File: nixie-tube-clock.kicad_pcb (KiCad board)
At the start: 2 copper layers, 157.5 x 72 mm, 137 parts, among them IC1 TPS61041DBVR, IC2 UCC3803DTR, J5 USB4105-GF-A, J7 DEBUG, Q1 MMBT42, Q2 FDS2672CT, SW1 SW_SPST, U1 CD40109BPW, U2 W25Q32JV, U3 RP2350A, U4 MCP1702T-3302E_CB, U5 CD40109BPW, U6 HV5122PG-G, U7 HV5122PG-G, U8 DS3231M, X1 IQXO-791

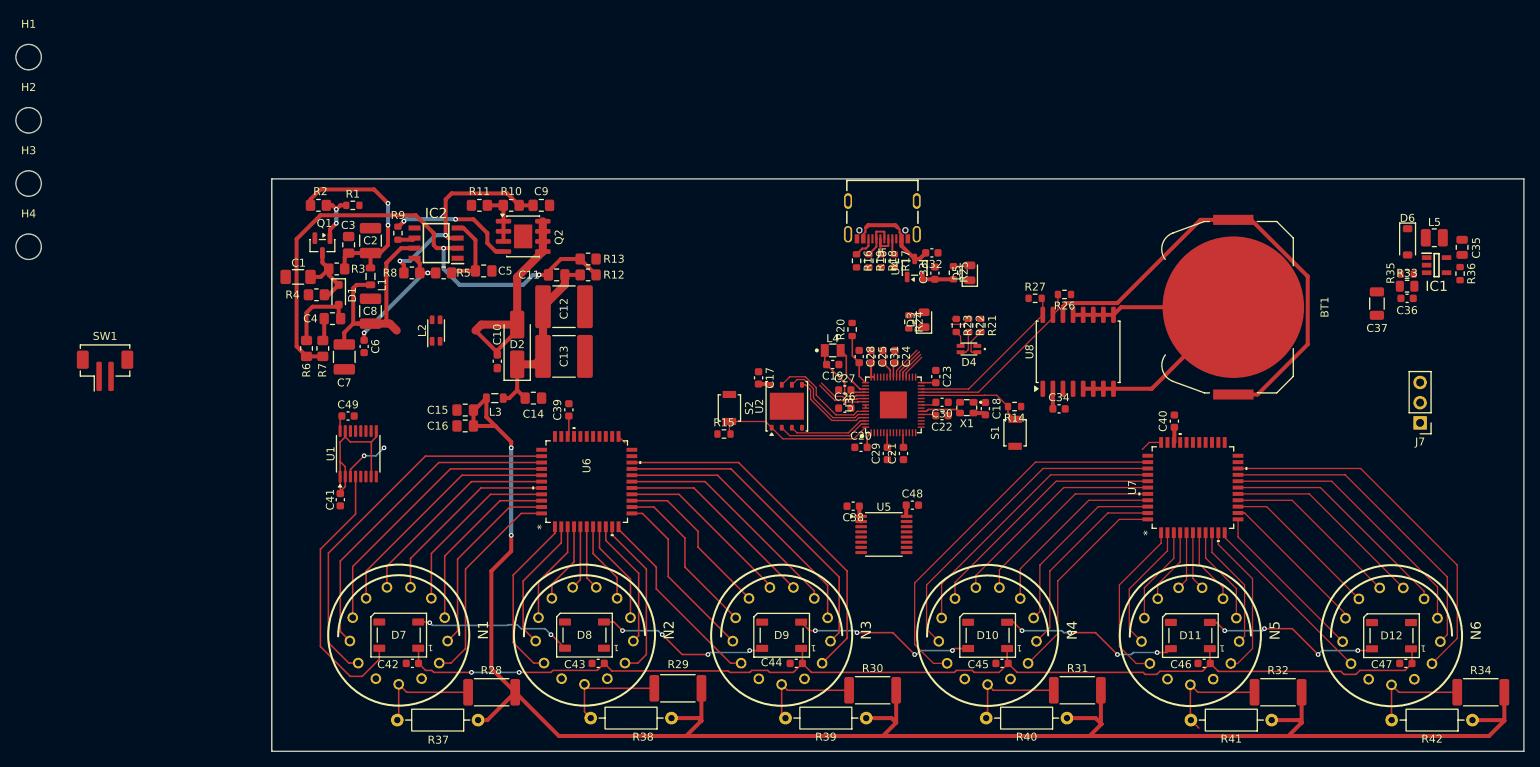
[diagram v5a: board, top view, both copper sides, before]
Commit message: Complete layout first pass
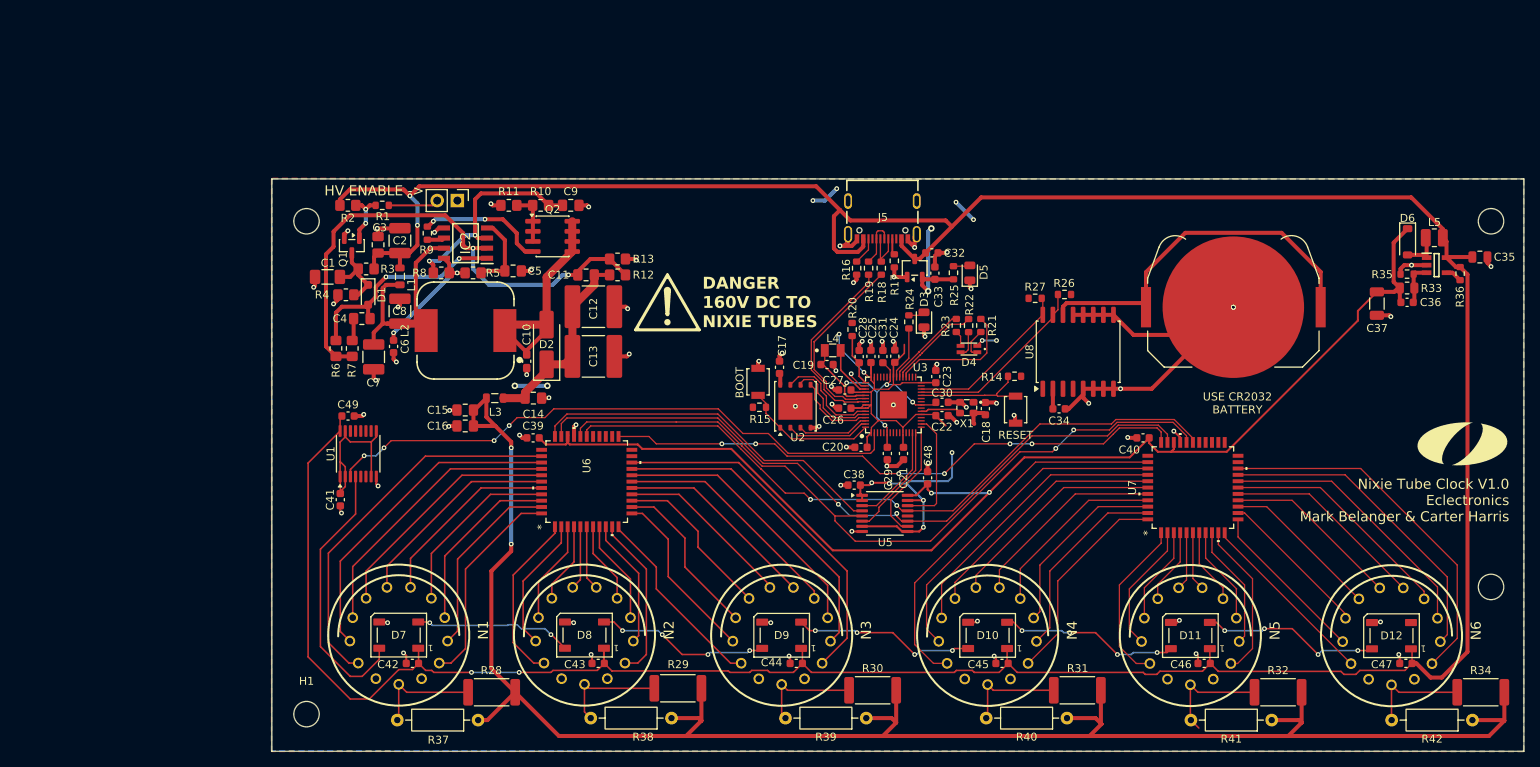
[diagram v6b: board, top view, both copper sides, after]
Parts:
- removed J7: DEBUG, Connector_PinHeader_2.54mm:PinHeader_1x03_P2.54mm_Vertical
- removed S1: RST, Button_Switch_SMD:SW_SPST_B3U-1000P
- removed S2: BOOT, Button_Switch_SMD:SW_SPST_B3U-1000P
- added BOOT: BOOT, Button_Switch_SMD:SW_SPST_B3U-1000P, F.Cu at (175.8, 67.2)
- added OlinLogoLg: G***, Eclectronics:OlinLogoLg, F.Cu at (264.4, 75.0)
- added REF**: Symbol_Attention_Triangle_8x7mm_Copper, Symbol:Symbol_Attention_Triangle_8x7mm_Copper, F.Cu at (164.4, 57.2)
- added RESET: RST, Button_Switch_SMD:SW_SPST_B3U-1000P, F.Cu at (208.2, 70.7)
- added svg2mod: G***, Eclectronics:OlinLogoHuge, F.Cu at (229.3, 65.6)
- C38, C39, C40, C41, C42, C43, C44, C45, C46, C47, C48, C49: value 0.1uF -> 0.1µF
- L2: footprint Inductor_SMD:L_CommonMode_Wurth_WE-CNSW-1206 -> eclectronics_nixie_footprints:WE-PD_1210
- Q2: footprint Package_SO:SOIC-8-1EP_3.9x4.9mm_P1.27mm_EP2.29x3mm -> Package_SO:SOIC-8_3.9x4.9mm_P1.27mm
- SW1: footprint Connector_JST:JST_ZH_B2B-ZR-SM4-TF_1x02-1MP_P1.50mm_Vertical -> Connector_PinHeader_2.54mm:PinHeader_1x02_P2.54mm_Vertical
- moved H2 193.1 mm to (268.0, 93.0)
- moved H3 184.0 mm to (268.0, 47.0)
- moved H1 89.7 mm to (119.0, 109.0)
- moved SW1 49.2 mm to (138.0, 44.4), turned to -90 degrees
- moved H4 35.1 mm to (119.0, 47.0)
- moved C39 5.72 mm to (147.5, 74.2), turned to 180 degrees
- moved R15 5.59 mm to (176.0, 70.4)
- moved C40 4.47 mm to (224.2, 74.2), turned to 180 degrees
- moved C48 3.94 mm to (197.1, 79.3), turned to 90 degrees
- moved R14 3.81 mm to (208.1, 66.5)
- moved C12 3.70 mm to (155.1, 57.8)
- moved C13 3.70 mm to (155.1, 64.0)
- moved C5 3.70 mm to (145.0, 53.2)
- moved C9 3.70 mm to (152.2, 45.0)
- moved C1 3.70 mm to (121.6, 54.0)
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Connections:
- C38 pad 1: 3V3 -> +3V3
- C41 pad 1: 3V3 -> +3V3
- U1 pad 1: 3V3 -> +3V3
- U1 pad 15: 3V3 -> +3V3
- U1 pad 2: 3V3 -> +3V3
- U1 pad 7: 3V3 -> +3V3
- U1 pad 9: 3V3 -> +3V3
- U3 pad 14: SR_CLK_3V3 -> SR_DATA_IN_3V3
- U3 pad 15: SR_DATA_IN_3V3 -> SR_CLK_3V3
- U3 pad 18: LED_LOGIC_3V3 -> unconnected-(U3-GPIO14-Pad18)
- U3 pad 2: unconnected-(U3-GPIO0-Pad2) -> LED_LOGIC_3V3
- U5 pad 1: 3V3 -> +3V3
- U5 pad 15: 3V3 -> +3V3
- U5 pad 2: 3V3 -> +3V3
- U5 pad 7: 3V3 -> +3V3
- U5 pad 9: 3V3 -> +3V3
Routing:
- net +5V: track 180.8 -> 441.4 mm
- net +12V: track 5.99 -> 155.9 mm, vias 0 -> 2
- net +3V3: track 24.0 -> 148.0 mm, vias 0 -> 17
- net GND: track 43.7 -> 154.4 mm, vias 0 -> 74
- net /nixie_tubes_driver/SR_CLK: track 0.00 -> 95.4 mm, vias 0 -> 2
- net /nixie_tubes_driver/SR_STR: track 0.00 -> 90.5 mm, vias 0 -> 2
- net /nixie_tubes_driver/SR_OE: track 0.00 -> 88.0 mm, vias 0 -> 2
- net /nixie_tubes_driver/SR_DATA: track 3.89 -> 74.1 mm, vias 0 -> 6
- net LED_LOGIC_3V3: track 6.24 -> 74.6 mm, vias 2 -> 4
- net /nixie_tubes_driver/SR_DATA_IN: track 0.00 -> 45.6 mm
- net 3V3: track 25.0 -> 0.00 mm
- net +1V1: track 15.0 -> 34.2 mm, vias 0 -> 4
- net Net-(D1-A): track 9.82 -> 27.9 mm, vias 0 -> 2
- net Net-(U3-USB_D-): track 6.42 -> 24.0 mm
- net Net-(U3-USB_D+): track 6.67 -> 24.0 mm
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- added copper zone on F.Cu, net +3V3
- added copper zone on B.Cu, net GND
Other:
- board text added: "DANGER 160V DC TO NIXIE TUBES"
- board text added: "HV ENABLE ->"
- board text added: "Nixie Tube Clock V1.0 Eclectronics Mark Belanger & Carter Harris"
- board text added: "USE CR2032 BATTERY"

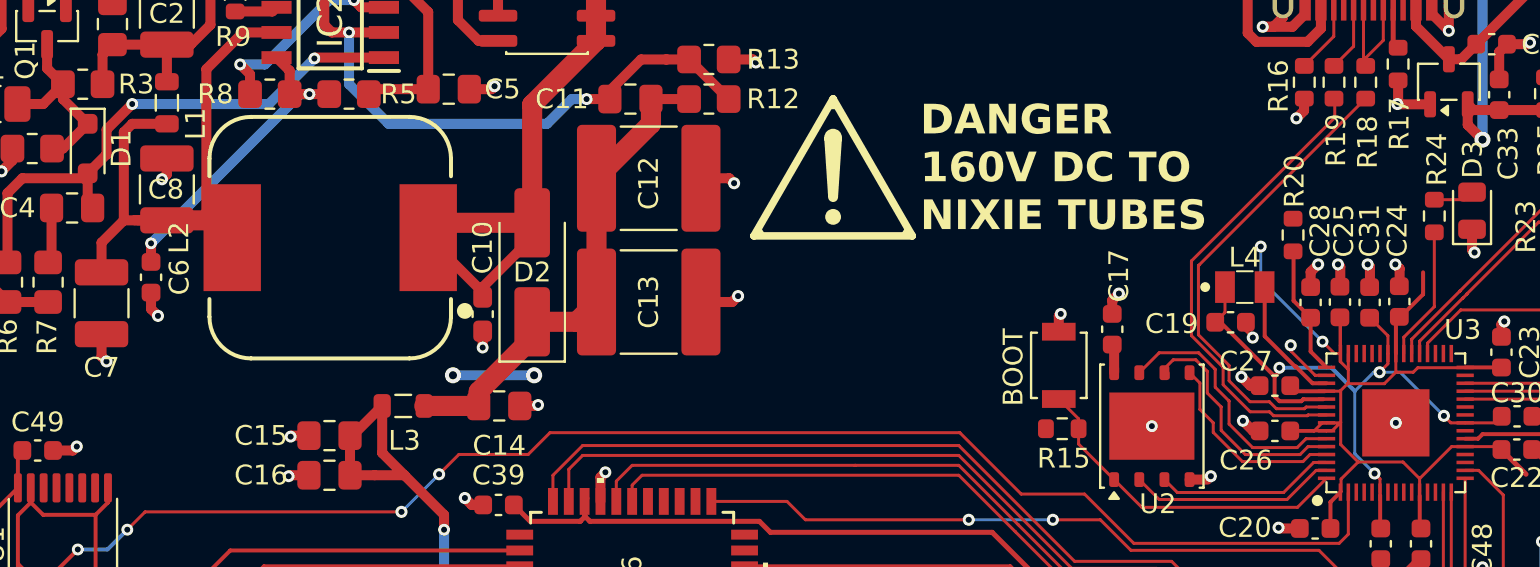
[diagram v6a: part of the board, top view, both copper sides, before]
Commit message: Add small schematic/layout changes
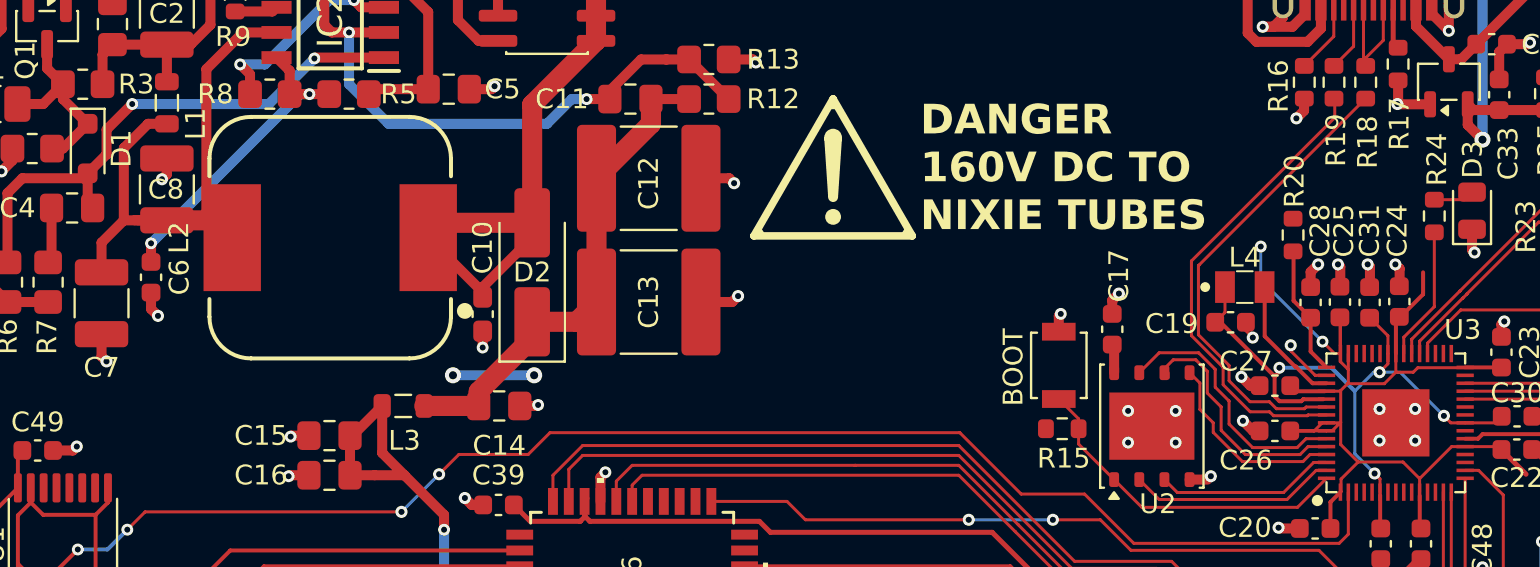
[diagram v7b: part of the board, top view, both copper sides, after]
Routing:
- net GND: vias 74 -> 80
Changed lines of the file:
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@@
 			(outputformat 1)
 			(mirror no)
-			(drillshape 1)
+			(drillshape 0)
 			(scaleselection 1)
-			(outputdirectory "")
+			(outputdirectory "gerbers/")
 		)
 	)
@@
 	)
 	(via
+		(at 181.7 69.5)
+		(size 0.6)
+		(drill 0.3)
+		(layers "F.Cu" "B.Cu")
+		(net 2)
+	)
+	(via
 		(at 119.9 55.3)
 		(size 0.6096)
@@
 	)
 	(via
+		(at 193.8 69.4)
+		(size 0.6096)
+		(drill 0.3048)
+		(layers "F.Cu" "B.Cu")
+		(net 2)
+	)
+	(via
 		(at 258 52.5228)
 		(size 0.6096)
@@
 	)
 	(via
+		(at 193.8 71)
+		(size 0.6096)
+		(drill 0.3048)
+		(layers "F.Cu" "B.Cu")
+		(net 2)
+	)
+	(via
 		(at 187.51494 66.18506)
 		(size 0.6096)
@@
 	)
 	(via
-		(at 192.8238 70.104)
+		(at 192 69.4)
 		(size 0.6096)
 		(drill 0.3048)
@@
 	)
 	(via
-		(at 124.2 48.2)
+		(at 192 71)
 		(size 0.6096)
 		(drill 0.3048)
@@
 	)
 	(via
-		(at 180.5 70.27)
-		(size 0.6)
-		(drill 0.3)
+		(at 124.2 48.2)
+		(size 0.6096)
+		(drill 0.3048)
 		(layers "F.Cu" "B.Cu")
 		(net 2)
@@
 	)
 	(via
+		(at 179.3 71.1)
+		(size 0.6)
+		(drill 0.3)
+		(layers "F.Cu" "B.Cu")
+		(net 2)
+	)
+	(via
 		(at 228.1 73.4)
 		(size 0.6096)
@@
 	)
 	(via
+		(at 181.7 71.1)
+		(size 0.6)
+		(drill 0.3)
+		(layers "F.Cu" "B.Cu")
+		(net 2)
+	)
+	(via
 		(at 187.6 86)
 		(size 0.6096)
@@
 	)
 	(via
+		(at 179.3 69.5)
+		(size 0.6)
+		(drill 0.3)
+		(layers "F.Cu" "B.Cu")
+		(net 2)
+	)
+	(via
 		(at 147.3 53.1)
 		(size 0.6096)
@@
 	)
 	(segment
+		(start 130.75 55)
+		(end 129.8 55)
+		(width 0.508)
+		(layer "F.Cu")
+		(net 9)
+	)
+	(segment
 		(start 129.125 59.875)
 		(end 128.575 59.875)
@@
 	)
 	(segment
-		(start 130.75 59.875)
-		(end 133.175 59.875)
-		(width 1.016)
+		(start 129.8 55)
+		(end 128.575 56.225)
+		(width 0.508)
 		(layer "F.Cu")
 		(net 9)
 	)
 	(segment
-		(start 129 55)
-		(end 128.575 55.425)
-		(width 0.508)
+		(start 130.75 59.875)
+		(end 133.175 59.875)
+		(width 1.016)
 		(layer "F.Cu")
 		(net 9)
@@
 	)
 	(segment
-		(start 128.575 55.425)
-		(end 128.575 59.875)
-		(width 0.508)
-		(layer "F.Cu")
-		(net 9)
-	)
-	(segment
 		(start 133.175 59.875)
 		(end 134.05 60.75)
@@
 	)
 	(segment
-		(start 130.75 55)
-		(end 129 55)
-		(width 0.508)
-		(layer "F.Cu")
-		(net 9)
-	)
-	(segment
 		(start 132.745 59.445)
 		(end 134.05 60.75)
@@
 		(width 0.508)
 		(layer "F.Cu")
+		(net 9)
+	)
+	(segment
+		(start 128.575 56.225)
+		(end 128.575 59.875)
+		(width 0.508)
+		(layer "F.Cu")

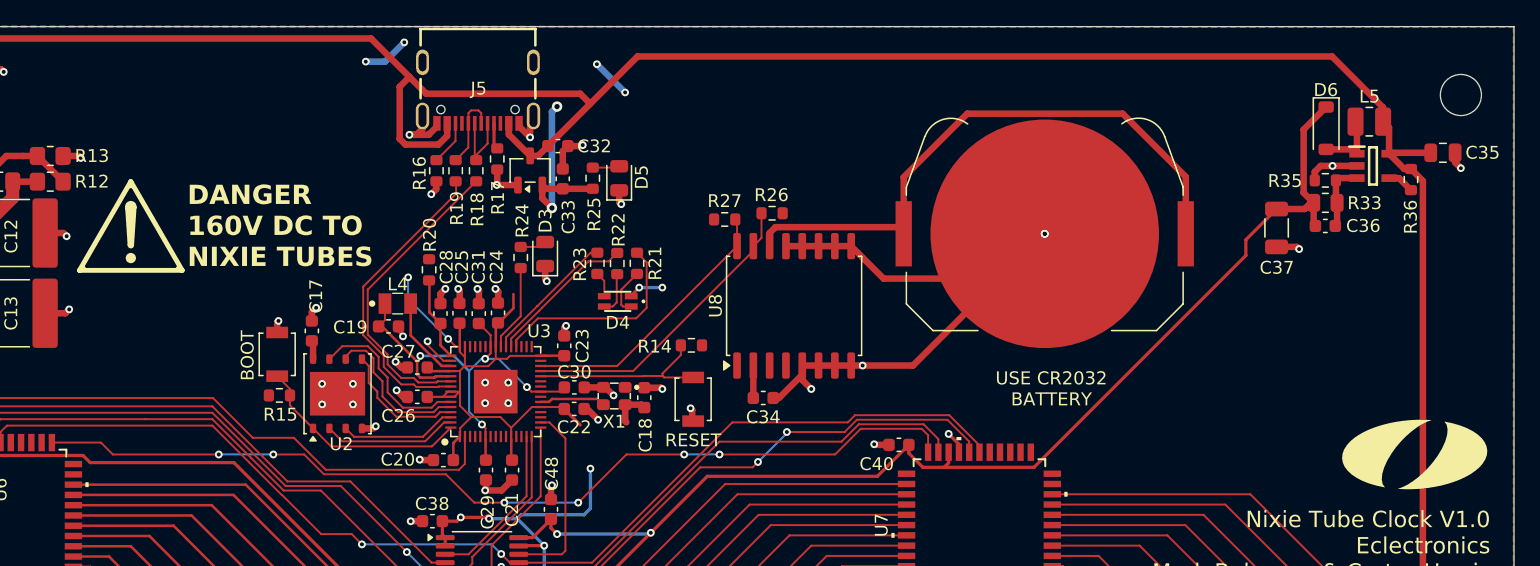
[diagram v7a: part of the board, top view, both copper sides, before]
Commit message: Add time set buttons
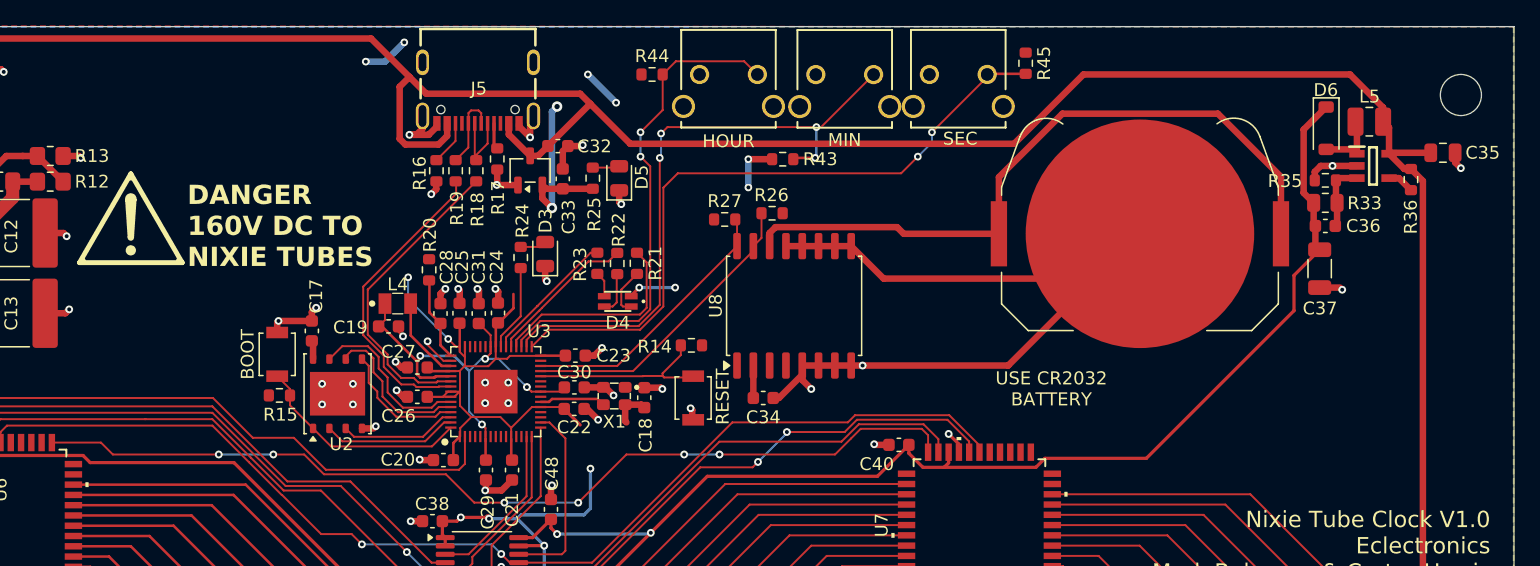
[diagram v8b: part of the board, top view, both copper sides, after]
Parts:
- removed OlinLogoLg: G***, Eclectronics:OlinLogoLg
- removed svg2mod: G***, Eclectronics:OlinLogoHuge
- added HOUR: 1825027-8, carter_kicad_footprints:SW2_1825027-C_TEC, F.Cu at (213.2, 45.4)
- added MIN: 1825027-8, carter_kicad_footprints:SW2_1825027-C_TEC, F.Cu at (222.3, 45.4)
- added R43: 10k, Resistor_SMD:R_0603_1608Metric, F.Cu at (215.2, 52.0)
- added R44: 10k, Resistor_SMD:R_0603_1608Metric, F.Cu at (205.0, 45.4)
- added R45: 10k, Resistor_SMD:R_0603_1608Metric, F.Cu at (234.1, 44.5)
- added SEC: 1825027-8, carter_kicad_footprints:SW2_1825027-C_TEC, F.Cu at (231.1, 45.4)
- moved BT1 7.41 mm to (243.0, 57.8)
- moved C37 4.62 mm to (257.0, 60.5)
- moved C23 1.16 mm to (199.0, 67.3), turned to 180 degrees
- moved REF** 0.60 mm to (164.4, 56.6)
- moved RESET 0.10 mm to (208.2, 70.6)
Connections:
- U3 pad 31: unconnected-(U3-GPIO19-Pad31) -> Net-(U3-GPIO19)
- U3 pad 32: unconnected-(U3-GPIO20-Pad32) -> Net-(U3-GPIO20)
- U3 pad 33: unconnected-(U3-GPIO21-Pad33) -> Net-(U3-GPIO21)
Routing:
- net Net-(U3-GPIO19): track 0.00 -> 53.3 mm, vias 0 -> 2
- net Net-(U3-GPIO20): track 0.00 -> 48.1 mm, vias 0 -> 4
- net Net-(U3-GPIO21): track 0.00 -> 39.1 mm, vias 0 -> 2
- net GND: track 154.4 -> 172.3 mm, vias 80 -> 78
- net Net-(BT1-+): track 46.8 -> 54.2 mm
- net +3V3: track 148.0 -> 153.1 mm, vias 17 -> 19
- net +12V: track 155.9 -> 157.6 mm
- net +5V: track 441.4 -> 442.8 mm
